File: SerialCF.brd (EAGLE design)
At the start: 106.7 x 49.2 mm, 19 parts, among them IC1 XR-16C550P, IC2 74LS138N, T1 BC547, T2 BC547

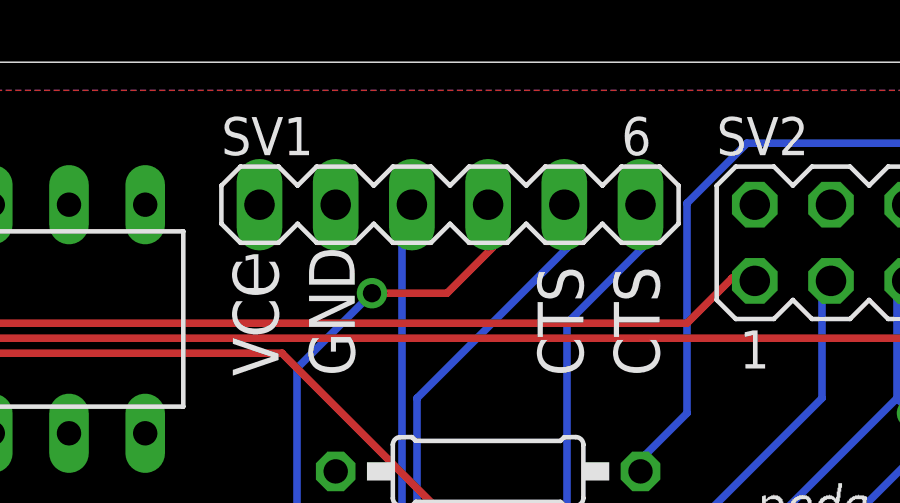
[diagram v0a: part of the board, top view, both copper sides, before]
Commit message: Rearrange Text on SerialCF Board
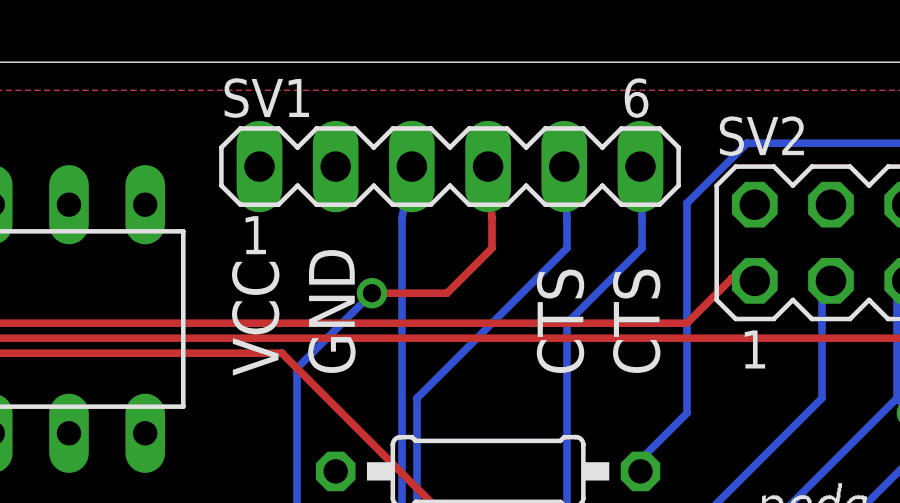
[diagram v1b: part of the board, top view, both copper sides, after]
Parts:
- moved SV1 1.27 mm to (38.1, 45.7)
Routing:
- net N$14: track 35.6 -> 36.9 mm
- net N$12: track 48.4 -> 49.7 mm
- net N$11: track 22.0 -> 23.2 mm
- net N$15: track 18.3 -> 19.5 mm
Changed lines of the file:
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@@
 <attribute name="SPICEMODEL" value="NONE" x="39.37" y="35.56" size="1.778" layer="27" rot="R180" display="off"/>
 </element>
-<element name="SV1" library="con-lstb" package="MA06-1" value="SERIAL" x="38.1" y="44.45" smashed="yes">
-<attribute name="MF" value="" x="38.1" y="44.45" size="1.778" layer="27" display="off"/>
-<attribute name="MPN" value="" x="38.1" y="44.45" size="1.778" layer="27" display="off"/>
-<attribute name="OC_NEWARK" value="unknown" x="38.1" y="44.45" size="1.778" layer="27" display="off"/>
-<attribute name="OC_FARNELL" value="unknown" x="38.1" y="44.45" size="1.778" layer="27" display="off"/>
-<attribute name="NAME" x="30.48" y="46.101" size="1.27" layer="25" ratio="10"/>
+<element name="SV1" library="con-lstb" package="MA06-1" value="SERIAL" x="38.1" y="45.72" smashed="yes">
+<attribute name="MF" value="" x="38.1" y="45.72" size="1.778" layer="27" display="off"/>
+<attribute name="MPN" value="" x="38.1" y="45.72" size="1.778" layer="27" display="off"/>
+<attribute name="OC_NEWARK" value="unknown" x="38.1" y="45.72" size="1.778" layer="27" display="off"/>
+<attribute name="OC_FARNELL" value="unknown" x="38.1" y="45.72" size="1.778" layer="27" display="off"/>
+<attribute name="NAME" x="30.48" y="47.371" size="1.27" layer="25" ratio="10"/>
 </element>
 <element name="SV2" library="con-lstb" package="MA20-2" value="IDE PATA CF Card" x="72.39" y="43.18">
@@
 <contactref element="QG1" pad="14"/>
 <contactref element="SV1" pad="1"/>
-<wire x1="34.29" y1="35.56" x2="31.75" y2="44.45" width="0" layer="19" extent="1-1"/>
+<wire x1="34.29" y1="35.56" x2="31.75" y2="45.72" width="0" layer="19" extent="1-1"/>
 <wire x1="65.405" y1="30.48" x2="78.74" y2="36.83" width="0" layer="19" extent="1-1"/>
 </signal>
@@
 <wire x1="39.5" y1="44" x2="39.5" y2="43" width="0.254" layer="1"/>
 <wire x1="33" y1="27" x2="33.02" y2="26.67" width="0.254" layer="16"/>
-<wire x1="39.5" y1="44" x2="39.37" y2="44.45" width="0.254" layer="1"/>
+<wire x1="39.5" y1="44" x2="39.37" y2="45.72" width="0.254" layer="1"/>
 <via x="35.5" y="41.5" extent="1-16" drill="0.6096"/>
 </signal>
@@
 <wire x1="36.5" y1="44" x2="36.5" y2="29" width="0.254" layer="16"/>
 <wire x1="36" y1="27" x2="35.56" y2="26.67" width="0.254" layer="16"/>
-<wire x1="36.5" y1="44" x2="36.83" y2="44.45" width="0.254" layer="16"/>
+<wire x1="36.5" y1="44" x2="36.83" y2="45.72" width="0.254" layer="16"/>
 </signal>
 <signal name="IOCS1">
@@
 <wire x1="42" y1="44" x2="42" y2="43" width="0.254" layer="16"/>
 <wire x1="48" y1="11" x2="48.26" y2="11.43" width="0.254" layer="16"/>
-<wire x1="42" y1="44" x2="41.91" y2="44.45" width="0.254" layer="16"/>
+<wire x1="42" y1="44" x2="41.91" y2="45.72" width="0.254" layer="16"/>
 </signal>
 <signal name="N$14">
@@
 <wire x1="44.5" y1="44" x2="44.5" y2="43" width="0.254" layer="16"/>
 <wire x1="40.5" y1="11.5" x2="40.64" y2="11.43" width="0.254" layer="16"/>
-<wire x1="44.5" y1="44" x2="44.45" y2="44.45" width="0.254" layer="16"/>
+<wire x1="44.5" y1="44" x2="44.45" y2="45.72" width="0.254" layer="16"/>
 </signal>
 </signals>

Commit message: Fix Routing Issues with PowerPlanes
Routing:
- net VCC: track 0.00 -> 9.53 mm, vias 0 -> 4
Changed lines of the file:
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@@
 <element name="C4" library="capacitor-wima" package="C5B2.5" value="0.1µF" x="81.28" y="36.83" smashed="yes">
 <attribute name="NAME" x="75.438" y="35.814" size="1.27" layer="25" ratio="10"/>
-<attribute name="VALUE" x="79.248" y="34.036" size="1.27" layer="27" ratio="10"/>
+<attribute name="VALUE" x="80.518" y="34.036" size="1.27" layer="27" ratio="10"/>
 </element>
 <element name="T2" library="transistor" package="TO92" value="BC547" x="72.39" y="30.48"/>
@@
 <contactref element="QG1" pad="14"/>
 <contactref element="SV1" pad="1"/>
-<wire x1="34.29" y1="35.56" x2="30.48" y2="26.67" width="0" layer="19" extent="1-1"/>
-<wire x1="65.405" y1="30.48" x2="78.74" y2="36.83" width="0" layer="19" extent="1-1"/>
+<via x="79.375" y="34.29" extent="1-16" drill="0.6"/>
+<wire x1="79.375" y1="34.29" x2="77.47" y2="34.29" width="0.4064" layer="16"/>
+<wire x1="77.47" y1="34.29" x2="77.47" y2="30.48" width="0.4064" layer="16"/>
+<via x="77.47" y="30.48" extent="1-16" drill="0.6"/>
+<via x="29.21" y="33.655" extent="1-16" drill="0.6"/>
+<via x="29.21" y="29.845" extent="1-16" drill="0.6"/>
+<wire x1="29.21" y1="33.655" x2="29.21" y2="29.845" width="0.4064" layer="16"/>
 </signal>
 <signal name="GND">

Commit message: Fix stupid VCC/GND mistakes on Address decoder
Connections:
- net GND: no longer IC2.6
- net VCC: now also IC2.6
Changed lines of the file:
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@@
 <via x="29.21" y="29.845" extent="1-16" drill="0.6"/>
 <wire x1="29.21" y1="33.655" x2="29.21" y2="29.845" width="0.4064" layer="16"/>
+<contactref element="IC2" pad="6"/>
 </signal>
 <signal name="GND">
@@
 <contactref element="JP1" pad="80"/>
 <contactref element="IC2" pad="8"/>
-<contactref element="IC2" pad="6"/>
 <contactref element="QG1" pad="7"/>
 <contactref element="SV1" pad="2"/>

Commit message: Add pullup
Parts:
- added R7: 3.3k, resistor:0207/2V
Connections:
- net !RESET: now also R7.1
- net IOCS1: now also IC2.15
- net N$5: now also IC2.5
- net VCC: now also R7.2
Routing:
- net !RESET: track 78.0 -> 80.5 mm
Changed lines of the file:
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@@
 <attribute name="OC_FARNELL" value="unknown" x="85.09" y="15.24" size="1.778" layer="27" display="off"/>
 </element>
+<element name="R7" library="resistor" package="0207/2V" value="3.3k" x="5.08" y="8.89"/>
 </elements>
 <signals>
@@
 <wire x1="29.21" y1="33.655" x2="29.21" y2="29.845" width="0.4064" layer="16"/>
 <contactref element="IC2" pad="6"/>
+<contactref element="R7" pad="2"/>
 </signal>
 <signal name="GND">
@@
 <wire x1="4" y1="6.5" x2="3.81" y2="6.35" width="0.254" layer="1"/>
 <wire x1="48" y1="42" x2="48.26" y2="41.91" width="0.254" layer="1"/>
+<contactref element="R7" pad="1"/>
+<wire x1="3.81" y1="6.35" x2="3.81" y2="8.89" width="0.4064" layer="1"/>
 </signal>
 <signal name="N$11">
@@
 <signal name="IOCS1">
 <contactref element="SV2" pad="37"/>
+<contactref element="IC2" pad="15"/>
+<wire x1="12.7" y1="44.45" x2="93.98" y2="41.91" width="0" layer="19" extent="1-1"/>
 </signal>
 <signal name="N$20">
@@
 <signal name="N$5">
 <contactref element="JP1" pad="59"/>
+<contactref element="IC2" pad="5"/>
+<wire x1="29.21" y1="6.35" x2="20.32" y2="36.83" width="0" layer="19" extent="1-1"/>
 </signal>
 <signal name="N$6">
